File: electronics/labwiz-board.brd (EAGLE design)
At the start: 98.8 x 51 mm, 96 parts, among them J1 SD_MICRO_SDIO_1BIT, J2 CORTEX_DEBUGSMD, J3 DNP, U1 STM32F10XRXT6, U2 MCP73831/2, U4 MIC5219-3.3V, X2 M12_BOTTOM_CONTACTS_FPC_1MM, Y3 32.768kHz

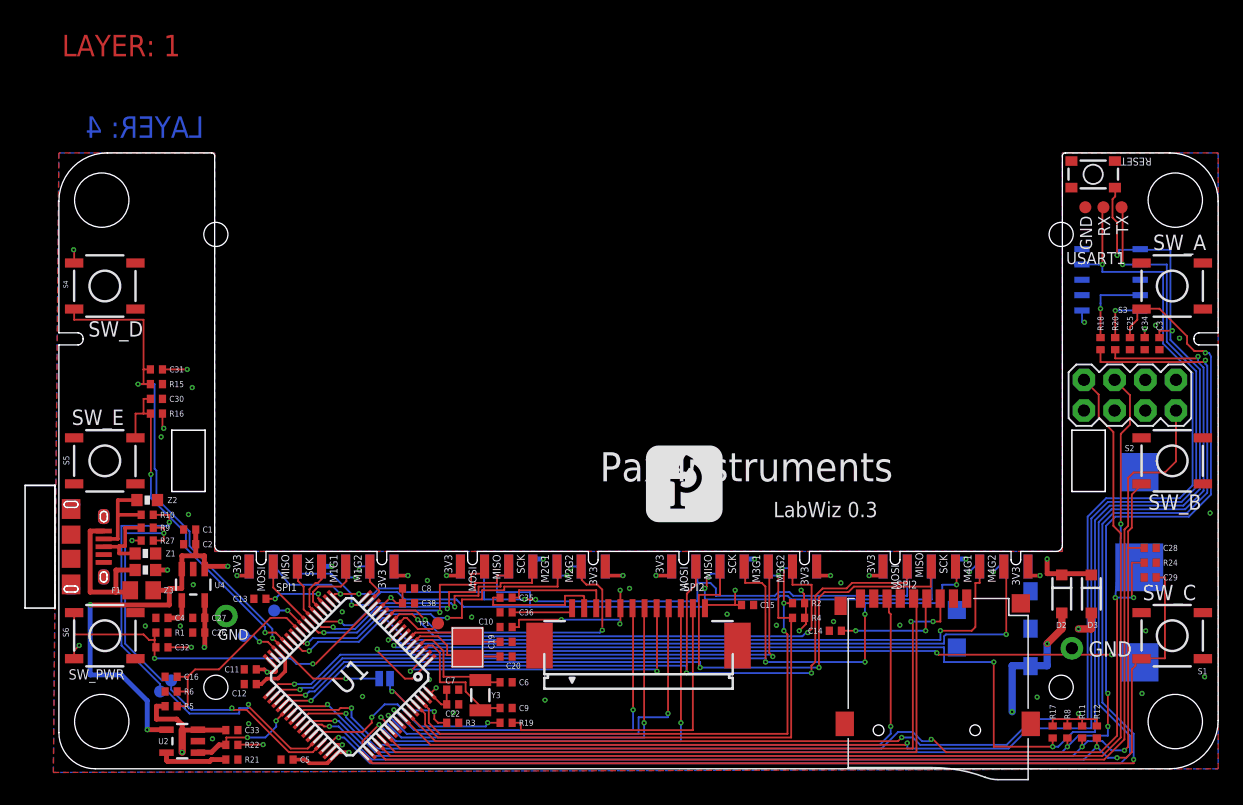
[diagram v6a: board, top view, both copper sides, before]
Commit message: Added 100k pullup resistors to the USART1 lines. Closes #26.
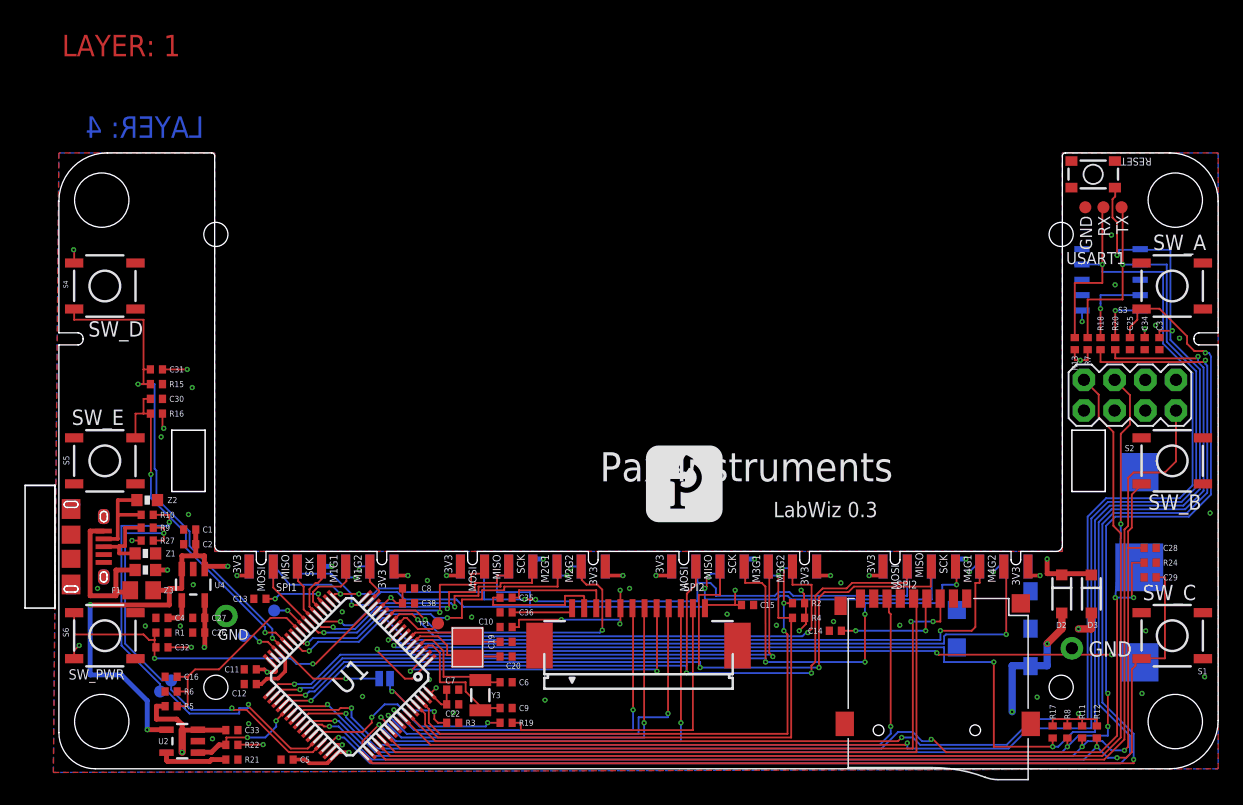
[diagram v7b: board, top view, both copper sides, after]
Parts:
- added R13, R7: 100K, PaxInstruments-RCL:0402
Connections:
- net 3.3V: now also R13.1, R7.1
- net USART1_RX: now also R13.2
- net USART1_TX: now also R7.2
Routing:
- net USART1_TX: track 114.0 -> 122.9 mm
- net USART1_RX: track 116.3 -> 124.6 mm
- net 3.3V: track 93.3 -> 96.0 mm, vias 34 -> 35
- net USB_VCC: track 13.1 -> 13.7 mm
- net GND: vias 30 -> 33
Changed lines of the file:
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@@
 <attribute name="NAME" x="8.6868" y="14.7828" size="0.5" layer="25" font="vector" align="center-left"/>
 </element>
+<element name="R7" library="PaxInstruments-RCL" package="0402" value="100K" x="85.1916" y="35.2044" rot="R90"/>
+<element name="R13" library="PaxInstruments-RCL" package="0402" value="100K" x="84.1248" y="35.2044" rot="R90"/>
 </elements>
 <signals>
@@
 <wire x1="46.5" y1="13.2975" x2="46.5" y2="14.7648" width="0.1524" layer="1"/>
 <wire x1="46.5" y1="14.7648" x2="46.482" y2="14.7828" width="0.1524" layer="1"/>
-<via x="84.9296" y="36.9784" extent="1-16" drill="0.2"/>
+<via x="84.7344" y="37.0332" extent="1-16" drill="0.2"/>
 <wire x1="84.7194" y1="37.952" x2="84.7238" y2="37.9476" width="0.1524" layer="16"/>
 <wire x1="84.7238" y1="37.9476" x2="84.7344" y2="36.9784" width="0.1524" layer="16"/>
-<wire x1="84.7344" y1="36.9784" x2="84.9296" y2="36.9784" width="0.1524" layer="16"/>
+<wire x1="84.7344" y1="36.9784" x2="84.7344" y2="37.0332" width="0.1524" layer="16"/>
 <wire x1="16.3496" y1="8.2296" x2="17.0204" y2="8.2296" width="0.3048" layer="1"/>
 <wire x1="17.0204" y1="8.2296" x2="17.25" y2="8" width="0.3048" layer="1"/>
@@
 <wire x1="38.1" y1="11.7348" x2="38.1" y2="12.3444" width="0.1524" layer="1"/>
 <wire x1="38.1" y1="12.3444" x2="41.6052" y2="12.3444" width="0.1524" layer="1"/>
+<contactref element="R13" pad="1"/>
+<contactref element="R7" pad="1"/>
+<via x="84.582" y="33.8328" extent="1-16" drill="0.2"/>
+<wire x1="84.1248" y1="34.7044" x2="84.1248" y2="33.8328" width="0.1524" layer="1"/>
+<wire x1="84.1248" y1="33.8328" x2="84.582" y2="33.8328" width="0.1524" layer="1"/>
+<wire x1="85.1916" y1="34.7044" x2="85.1916" y2="33.8328" width="0.1524" layer="1"/>
+<wire x1="85.1916" y1="33.8328" x2="84.582" y2="33.8328" width="0.1524" layer="1"/>
 </signal>
 <signal name="GND" class="5">
@@
 <via x="8.9916" y="16.4592" extent="1-16" drill="0.2"/>
 <wire x1="8.0128" y1="16.4592" x2="8.9916" y2="16.4592" width="0.4064" layer="1"/>
-<wire x1="3.71" y1="15.888" x2="3.71" y2="15.888" width="0" layer="19" extent="1-16"/>
+<via x="87.4656" y="40.0812" extent="1-16" drill="0.2"/>
+<via x="87.1608" y="44.196" extent="1-16" drill="0.2"/>
+<via x="3.2004" y="14.9352" extent="1-16" drill="0.2"/>
 </signal>
 <signal name="N$3">
@@
 <contactref element="U$1" pad="PIN$1"/>
 <wire x1="3.71" y1="19.688" x2="2.5908" y2="19.688" width="0.4064" layer="1"/>
-<wire x1="2.5908" y1="19.688" x2="2.5908" y2="14.6304" width="0.4064" layer="1"/>
-<wire x1="2.5908" y1="14.6304" x2="4.7244" y2="14.6304" width="0.4064" layer="1"/>
+<wire x1="2.5908" y1="19.688" x2="2.5908" y2="14.3256" width="0.4064" layer="1"/>
+<wire x1="2.5908" y1="14.3256" x2="4.7244" y2="14.3256" width="0.4064" layer="1"/>
+<wire x1="4.7244" y1="14.3256" x2="4.7244" y2="14.6304" width="0.4064" layer="1"/>
 <wire x1="4.7244" y1="14.6304" x2="5.9436" y2="14.6304" width="0.4064" layer="1"/>
 <wire x1="5.9436" y1="14.6304" x2="5.9436" y2="14.7828" width="0.4064" layer="1"/>
@@
 <wire x1="88.0872" y1="46.1772" x2="88" y2="46.2424" width="0.1524" layer="1"/>
 <wire x1="88" y1="46.2424" x2="88" y2="46.5" width="0.1524" layer="1"/>
+<contactref element="R7" pad="2"/>
+<wire x1="85.1916" y1="35.7044" x2="85.1916" y2="38.862" width="0.1524" layer="1"/>
+<wire x1="85.1916" y1="38.862" x2="88.0872" y2="38.862" width="0.1524" layer="1"/>
+<wire x1="88.0872" y1="38.862" x2="88.0872" y2="41.7576" width="0.1524" layer="1"/>
 </signal>
 <signal name="USART1_RX">
@@
 <contactref element="TP9" pad="P$1"/>
 <wire x1="86.4108" y1="46.4108" x2="86.5" y2="46.5" width="0.1524" layer="1"/>
+<contactref element="R13" pad="2"/>
+<wire x1="84.1248" y1="35.7044" x2="84.1248" y2="40.2336" width="0.1524" layer="1"/>
+<wire x1="84.1248" y1="40.2336" x2="86.4108" y2="40.2336" width="0.1524" layer="1"/>
+<wire x1="86.4108" y1="40.2336" x2="86.4108" y2="41.7576" width="0.1524" layer="1"/>
 </signal>
 <signal name="SWDIO_M">

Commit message: Added circuitry to alow PC1 to put BOOT0 into bootloader mode. I also had to switch around SW_E from normally high to normally low.
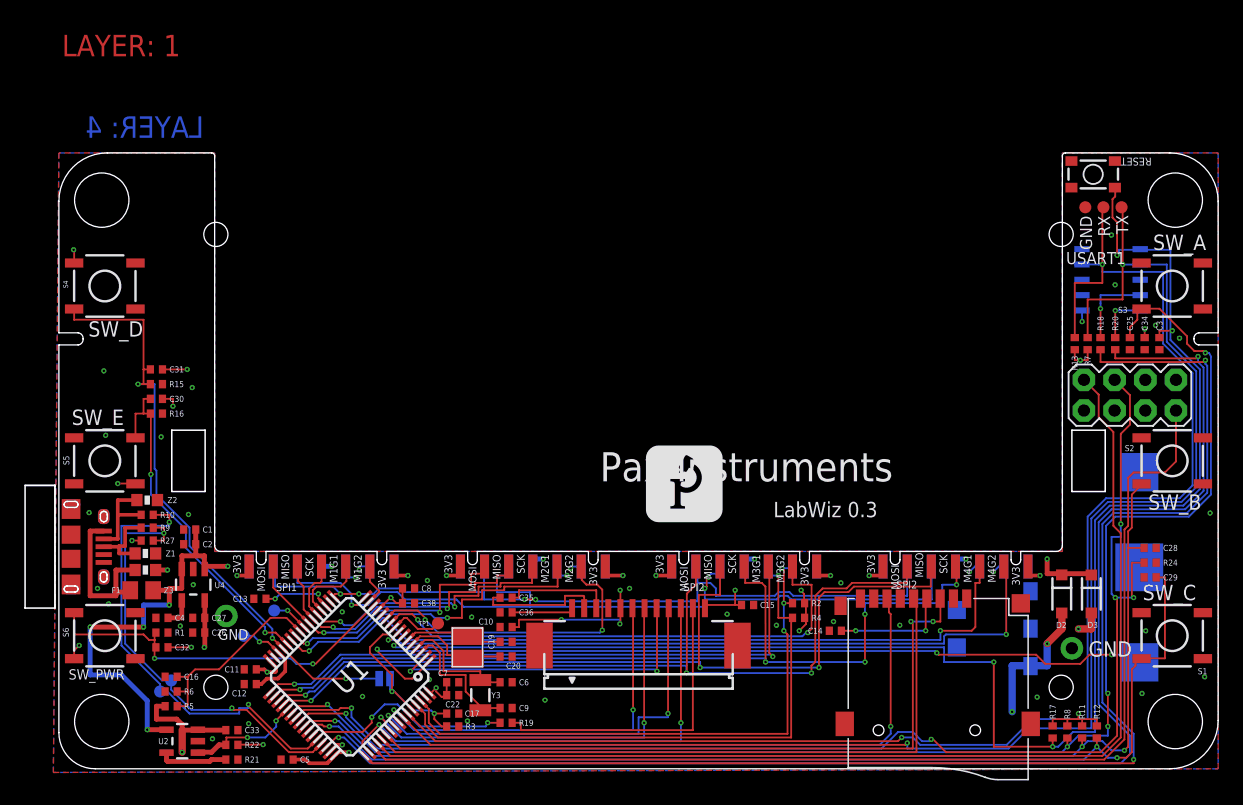
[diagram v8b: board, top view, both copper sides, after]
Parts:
- added C17: 1uF, PaxInstruments-RCL:0402
- moved C22 0.76 mm to (32.6, 6.10)
- moved C7 0.61 mm to (32.6, 7.16)
- moved R3 0.30 mm to (32.6, 3.51)
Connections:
- removed net BOOT0: JP1.2, R3.2, U1.60
- removed net PC1: TP1.P$1, U1.9
- new net PC1_BOOT0: C17.2, JP1.2, R3.2, TP1.P$1, U1.60, U1.9
- net 3.3V: now also C30.1, S5.1; no longer R16.1
- net GND: now also C17.1, R16.1; no longer C30.1, S5.1
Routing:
- net PC1_BOOT0: track 0.00 -> 22.2 mm, vias 0 -> 2
- net BOOT0: track 9.51 -> 0.00 mm, vias 2 -> 0
- net PC1: track 4.31 -> 0.00 mm
- net 3.3V: track 96.0 -> 97.2 mm, vias 35 -> 36
- net USART2_RX: track 63.8 -> 64.8 mm
- net WIFI_EN: track 107.5 -> 108.4 mm
- net RTC_BAT: track 70.1 -> 70.7 mm
- net VBUS: track 123.3 -> 123.2 mm, vias 8 -> 10
- net GND: vias 33 -> 36
